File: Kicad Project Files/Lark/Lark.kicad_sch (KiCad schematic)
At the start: 0 parts

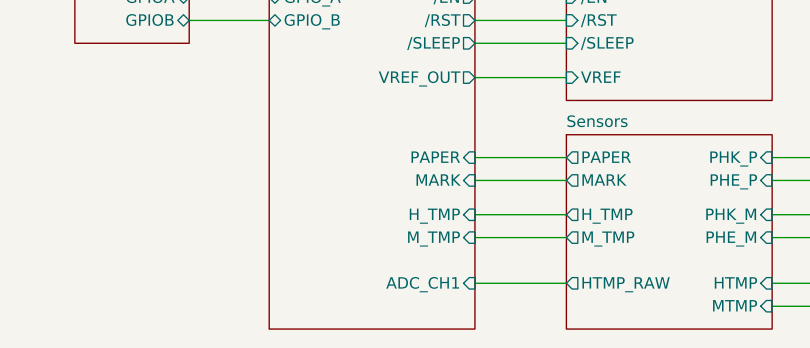
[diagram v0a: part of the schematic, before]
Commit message: fixed issue with ADC, Rev-ed board.
Turns out, you can in fact set PB5 to analog, but its use is with I2C1_SMBA, not the ADC, So I changed it to pin PA3. This renders the head temp functionality on revision 01.00.1 null.
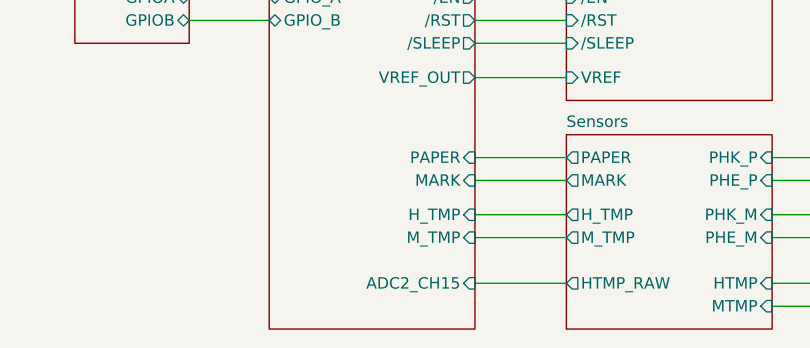
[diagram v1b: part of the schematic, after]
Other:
- sheet MCU ports: added ADC2_CH15; removed ADC_CH1
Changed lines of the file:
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@@
 		(title "Lark Print Engine")
 		(date "2025-10-08")
-		(rev "01.00.01")
+		(rev "01.00.02")
 		(comment 1 "Thermal Print Engine")
 		(comment 2 "Designer: HamSlices")
@@
 	(wire
 		(pts
+			(xy 128.27 135.89) (xy 138.43 135.89)
+		)
+		(stroke
+			(width 0)
+			(type default)
+		)
+	)
+	(wire
+		(pts
 			(xy 96.52 73.66) (xy 105.41 73.66)
 		)
@@
 	(wire
 		(pts
-			(xy 128.27 135.89) (xy 138.43 135.89)
-		)
-		(stroke
-			(width 0)
-			(type default)
-		)
-	)
-	(wire
-		(pts
 			(xy 128.27 71.12) (xy 170.18 71.12)
 		)
@@
 			)
 		)
-		(pin "ADC_CH1" input
+		(pin "ADC2_CH15" input
 			(at 128.27 135.89 0)
 			(effects
